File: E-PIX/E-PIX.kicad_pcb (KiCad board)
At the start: 6 copper layers, 40.1 x 45 mm, 65 parts, among them J1 USB_C_Receptacle_USB2.0, J2 DM3AT-SF-PEJM5, Q1 AO3401A, Q2 2SC4213, Q3 2SC4213, Q4 BSS138, Q5 BSS138, SW1 SW_Push, SW2 SW_Push, U10 ESP32-S3-WROOM-1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

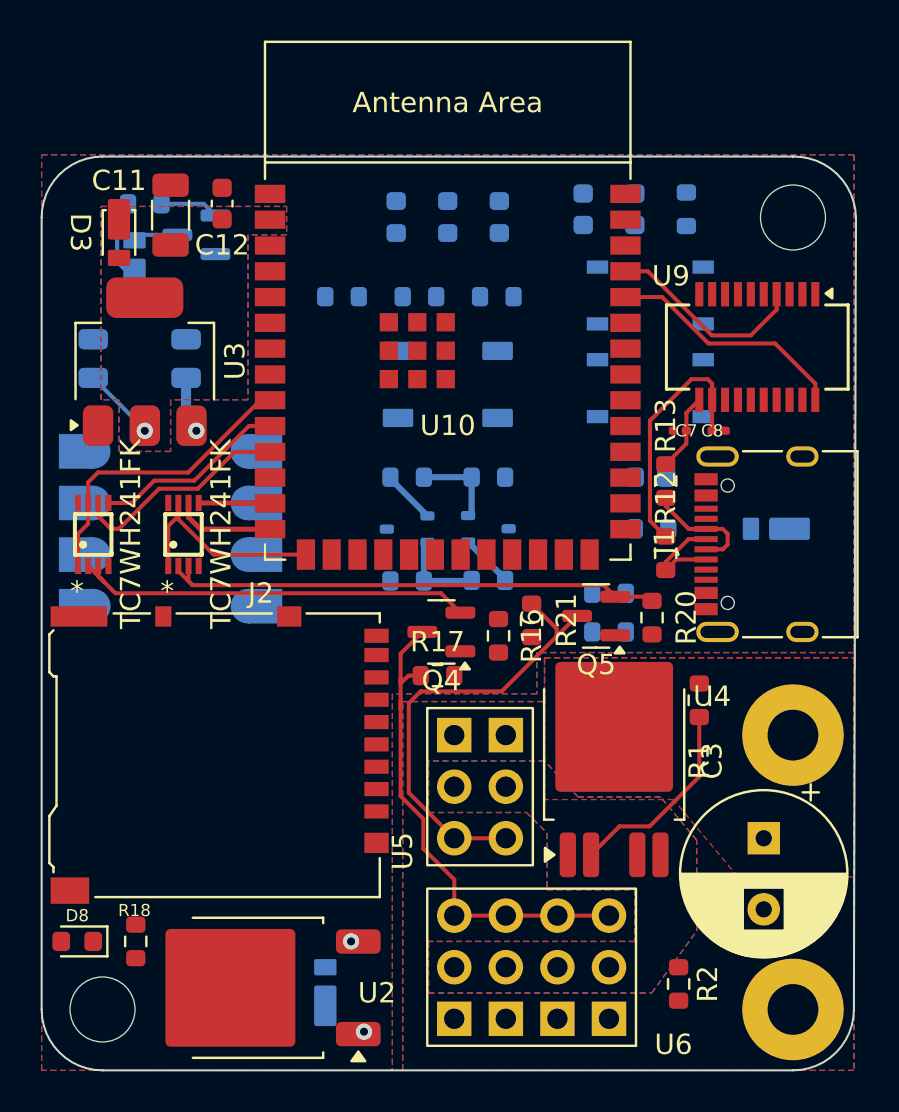
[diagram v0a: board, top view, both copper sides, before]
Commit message: successfly apply free routing
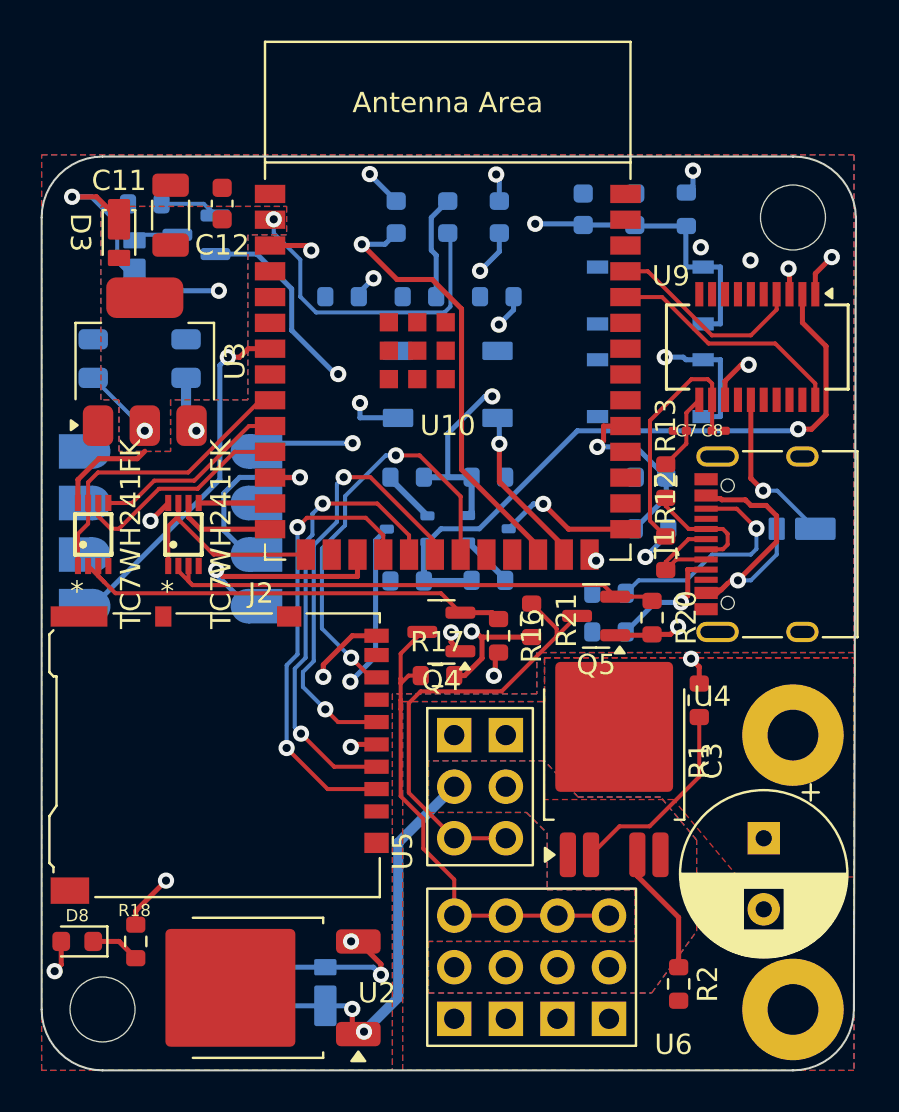
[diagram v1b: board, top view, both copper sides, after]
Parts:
- moved D5 1.27 mm to (162.8, 98.7)
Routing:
- net +3V3: track 3.66 -> 140.3 mm, vias 1 -> 16
- net VSS: track 8.08 -> 102.2 mm, vias 2 -> 6
- net +5V: track 0.00 -> 83.7 mm, vias 1 -> 5
- net /EN: track 0.00 -> 59.5 mm, vias 0 -> 3
- net /RTS: track 4.34 -> 33.0 mm, vias 0 -> 1
- net /DTR: track 4.31 -> 31.1 mm, vias 0 -> 2
- net /MOSI: track 0.00 -> 22.3 mm, vias 0 -> 2
- net /CS: track 0.00 -> 22.1 mm, vias 0 -> 2
- net /CLK: track 0.00 -> 21.9 mm, vias 0 -> 2
- net /led: track 0.00 -> 21.8 mm, vias 0 -> 1
- net /SW: track 0.00 -> 21.7 mm, vias 0 -> 2
- net /MISO: track 0.00 -> 20.9 mm, vias 0 -> 2
- net /SWA: track 0.00 -> 19.8 mm, vias 0 -> 2
- net /BNO_RST: track 0.00 -> 17.3 mm, vias 0 -> 1
- net Net-(D5-A): track 0.30 -> 15.2 mm, vias 0 -> 1
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
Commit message: create bear
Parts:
- moved D5 28.7 mm to (136.1, 88.4), turned to 0 degrees
- moved C1 3.86 mm to (131.9, 86.5)
- moved C5 3.86 mm to (127.3, 86.5)
- moved Q1 1.42 mm to (134.3, 83.6)
- moved R18 0.44 mm to (130.0, 118.6)
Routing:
- net +3V3: track 140.3 -> 176.5 mm, vias 16 -> 14
- net Net-(D5-A): track 15.2 -> 39.2 mm, vias 1 -> 2
- net VSS: track 102.2 -> 108.6 mm, vias 6 -> 28
- net Net-(J1-CC1): track 5.98 -> 12.1 mm
- net /SCL: track 10.6 -> 16.2 mm
- net Net-(D4-K): track 10.5 -> 5.28 mm, vias 2 -> 0
- net GND: track 0.00 -> 3.57 mm, vias 0 -> 95
- net Net-(Q1-G): track 3.30 -> 0.00 mm
- net /SDA: track 9.06 -> 6.40 mm
- net +5V: track 83.7 -> 81.1 mm, vias 5 -> 4
- net Net-(D7-K): track 8.43 -> 6.33 mm, vias 2 -> 0
- net /MISO: track 20.9 -> 22.6 mm
- net Net-(D1-A): track 2.22 -> 3.76 mm
- net /TX2: track 3.52 -> 4.20 mm
- net /DTR: track 31.1 -> 30.6 mm

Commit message: put silkscreen
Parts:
- added G***: LOGO, Logo:Robomech_05x05, B.Cu at (157.2, 109.9)
- added G***: LOGO, Logo:HRU_05x05, B.Cu at (152.3, 109.9)
- J1: footprint Connector_USB:USB_C_Receptacle_XKB_U262-16XN-4BVC11_with_model -> Conn:USB_C_Receptacle_XKB_U262-16XN-4BVC11_with_model
- SW1, SW2: footprint Button_Switch_SMD:SKRPACE010 -> Switch:SW_SKRPACE010
- U7: value TC7WH241FK -> U7
- U8: value TC7WH241FK -> U8
- renumbered U1 to BNO055, C10 to C1
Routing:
- net GND: track 3.57 -> 14.0 mm, vias 95 -> 157
- net VSS: track 108.6 -> 112.2 mm, vias 28 -> 27
- net /SCL: track 16.2 -> 12.8 mm
- net +5V: track 81.1 -> 77.8 mm
- net /SW: track 21.7 -> 18.9 mm
- net /EN: track 59.5 -> 56.9 mm
- net +3V3: track 176.5 -> 177.9 mm, vias 14 -> 24
- net /BNO_RST: track 17.3 -> 18.6 mm
- net /DTR: track 30.6 -> 31.5 mm
- net /RTS: track 33.0 -> 33.8 mm
- net Net-(U9-USBDM): track 12.3 -> 13.0 mm
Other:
- board text added: "E-PIX"
- board text added: "Robomech Factory Humanoid Robot Unit"
- board text added: "STATE"
- board text added: "SW"
- board text added: "main control board for humanoid"
- board text added: "v0 2025/12/15"

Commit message: create logo mark.
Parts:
- added G***: LOGO, Logo:E-PIX_05x05, F.Cu at (157.7, 82.7)
- added G***: LOGO, Logo:E-PIX_07x07, B.Cu at (138.4, 112.2)

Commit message: update silkscreen. ordered.
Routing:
- net GND: vias 157 -> 159
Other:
- board text added: "GND/VSS/ICS1"
- board text added: "ICS2/VSS/GND"
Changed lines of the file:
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@@
 		(tags "DPAK TO-252 DPAK-3 TO-252-3 SOT-428")
 		(property "Reference" "U2"
-			(at -5.955 -0.255 0)
+			(at -4.939 -0.001 0)
 			(layer "F.SilkS")
 			(effects
@@
 			(at -3.175 -1.27 0)
 			(layer "F.SilkS")
+			(hide yes)
 			(effects
 				(font
@@
 		(tags "resistor")
 		(property "Reference" "R17"
-			(at 1.461 -1.914 270)
+			(at 1.715 -0.009 270)
 			(layer "F.SilkS")
 			(effects
 				(font
-					(size 1 1)
-					(thickness 0.15)
+					(size 0.6 0.6)
+					(thickness 0.075)
 				)
 			)
@@
 			(at -2.54 5.715 90)
 			(layer "F.SilkS")
+			(hide yes)
 			(effects
 				(font
@@
 		)
 	)
+	(gr_line
+		(start 149.343 116.383)
+		(end 149.343 115.748)
+		(stroke
+			(width 0.125)
+			(type solid)
+		)
+		(layer "F.SilkS")
+	)
+	(gr_line
+		(start 154.483 116.383)
+		(end 154.483 115.748)
+		(stroke
+			(width 0.125)
+			(type solid)
+		)
+		(layer "F.SilkS")
+	)
+	(gr_line
+		(start 144.577 116.002)
+		(end 145.212 116.002)
+		(stroke
+			(width 0.125)
+			(type solid)
+		)
+		(layer "F.SilkS")
+	)
+	(gr_line
+		(start 149.343 115.748)
+		(end 148.708 115.748)
+		(stroke
+			(width 0.125)
+			(type solid)
+		)
+		(layer "F.SilkS")
+	)
+	(gr_line
+		(start 154.483 115.748)
+		(end 153.848 115.748)
+		(stroke
+			(width 0.125)
+			(type solid)
+		)
+		(layer "F.SilkS")
+	)
+	(gr_line
+		(start 146.803 116.383)
+		(end 146.803 115.748)
+		(stroke
+			(width 0.125)
+			(type solid)
+		)
+		(layer "F.SilkS")
+	)
+	(gr_line
+		(start 147.244 116.002)
+		(end 147.879 116.002)
+		(stroke
+			(width 0.125)
+			(type solid)
+		)
+		(layer "F.SilkS")
+	)
+	(gr_line
+		(start 146.803 115.748)
+		(end 146.168 115.748)
+		(stroke
+			(width 0.125)
+			(type solid)
+		)
+		(layer "F.SilkS")
+	)
+	(gr_line
+		(start 145.212 116.002)
+		(end 145.212 115.367)
+		(stroke
+			(width 0.125)
+			(type solid)
+		)
+		(layer "F.SilkS")
+	)
+	(gr_line
+		(start 151.883 116.383)
+		(end 151.883 115.748)
+		(stroke
+			(width 0.125)
+			(type solid)
+		)
+		(layer "F.SilkS")
+	)
+	(gr_line
+		(start 151.883 115.748)
+		(end 151.248 115.748)
+		(stroke
+			(width 0.125)
+			(type solid)
+		)
+		(layer "F.SilkS")
+	)
+	(gr_line
+		(start 147.879 116.002)
+		(end 147.879 115.367)
+		(stroke
+			(width 0.125)
+			(type solid)
+		)
+		(layer "F.SilkS")
+	)
+	(gr_line
+		(start 148.708 115.748)
+		(end 148.708 116.383)
+		(stroke
+			(width 0.125)
+			(type solid)
+		)
+		(layer "F.SilkS")
+	)
+	(gr_line
+		(start 153.848 115.748)
+		(end 153.848 116.383)
+		(stroke
+			(width 0.125)
+			(type solid)
+		)
+		(layer "F.SilkS")
+	)
+	(gr_line
+		(start 151.248 115.748)
+		(end 151.248 116.383)
+		(stroke
+			(width 0.125)
+			(type solid)
+		)
+		(layer "F.SilkS")
+	)
+	(gr_line
+		(start 144.577 115.367)
+		(end 144.577 116.002)
+		(stroke
+			(width 0.125)
+			(type solid)
+		)
+		(layer "F.SilkS")
+	)
+	(gr_line
+		(start 146.168 115.748)
+		(end 146.168 116.383)
+		(stroke
+			(width 0.125)
+			(type solid)
+		)
+		(layer "F.SilkS")
+	)
+	(gr_line
+		(start 147.244 115.367)
+		(end 147.244 116.002)
+		(stroke
+			(width 0.125)
+			(type solid)
+		)
+		(layer "F.SilkS")
+	)
 	(gr_arc
 		(start 162.4 80.4)
@@
 		(layer "Edge.Cuts")
 	)
+	(gr_text "GND/VSS/ICS1"
+		(at 144.196 123.749 90)
+		(layer "F.SilkS")
+		(effects
+			(font
+				(size 0.6 0.6)
+				(thickness 0.075)
+			)
+			(justify left bottom)
+		)
+	)
 	(gr_text "E-PIX"
 		(at 155.372 86.284 0)
@@
 		)
 	)
+	(gr_text "ICS2/VSS/GND"
+		(at 143.942 114.986 90)
+		(layer "F.SilkS")
+		(effects
+			(font
+				(size 0.6 0.6)
+				(thickness 0.075)
+			)
+			(justify left bottom)
+		)
+	)
 	(gr_text "E-PIX"
 		(at 136.322 114.224 0)
@@
 	)
 	(via
+		(at 144.196 107.62)
+		(size 0.8)
+		(drill 0.4)
+		(layers "F.Cu" "B.Cu")
+		(free yes)
+		(net 1)
+	)
+	(via
 		(at 164.77 87.935)
 		(size 0.8)
@@
 		(size 0.8)
 		(drill 0.4)
+		(layers "F.Cu" "B.Cu")
+		(free yes)
+		(net 1)
+	)
+	(via
+		(at 144.196 108.636)
+		(size 0.8)
+		(drill 0.4)
